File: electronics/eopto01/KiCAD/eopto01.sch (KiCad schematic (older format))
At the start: 7 parts, among them K1 CONN_3, Q1 BC849

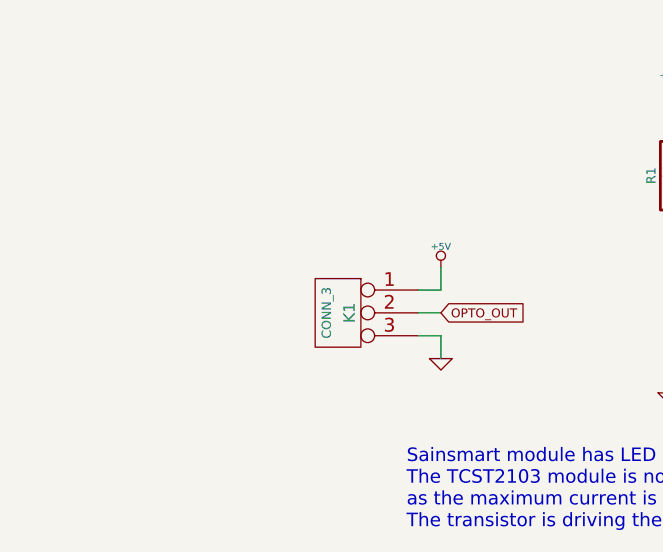
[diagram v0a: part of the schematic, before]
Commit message: Added JST connector for Opto-endstop
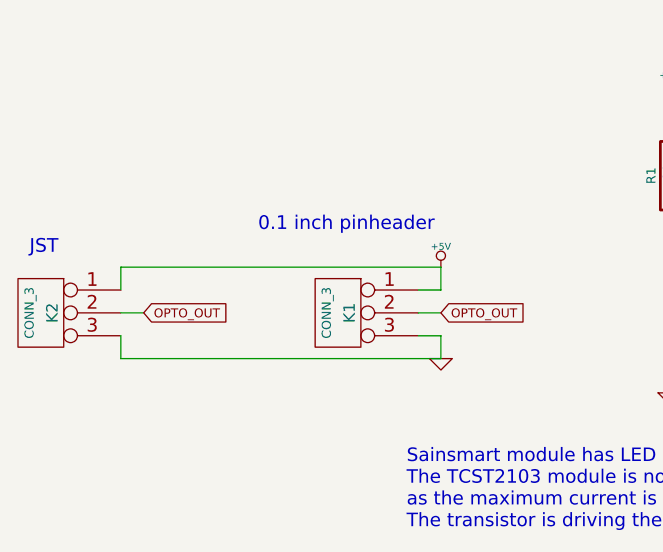
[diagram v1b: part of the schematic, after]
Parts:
- added K2: CONN_3, symbol CONN_3
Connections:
- net +5V: now also K2.1 (P1)
- net GND: now also K2.3 (P3)
- net OPTO_OUT: now also K2.2 (PM)
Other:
- note added: "0.1 inch pinheader"
- note added: "JST"
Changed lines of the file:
@@
 LIBS:valves
 LIBS:lerchetech
+LIBS:eopto01-cache
 EELAYER 27 0
 EELAYER END
@@
 Sheet 1 1
 Title "FirePick - Opto endstop board"
-Date "9 jul 2014"
+Date "12 jul 2014"
 Rev "A"
 Comp "FirePick"
@@
 Text Notes 4050 4750 0    59   ~ 0
 Sainsmart module has LED connected directly to opto-transistor output. \nThe TCST2103 module is not able to supply the current for the red LED, \nas the maximum current is 4mA @ 20mA forward current on the infrared LED. \nThe transistor is driving the LED, so when the light is interrupted, the LED lights up.
+$Comp
+L CONN_3 K2
+U 1 1 53C19586
+P 2450 3800
+F 0 "K2" V 2400 3800 50  0000 C CNN
+F 1 "CONN_3" V 2500 3800 40  0000 C CNN
+F 2 "" H 2450 3800 60  0000 C CNN
+F 3 "" H 2450 3800 60  0000 C CNN
+	1    2450 3800
+	-1   0    0    -1
+$EndComp
+Wire Wire Line
+	4200 3600 2800 3600
+Wire Wire Line
+	4200 4000 2800 4000
+Wire Wire Line
+	2800 3600 2800 3700
+Wire Wire Line
+	2800 4000 2800 3900
+Wire Wire Line
+	2800 3800 2900 3800
+Text GLabel 2900 3800 2    39   Input ~ 0
+OPTO_OUT
+Text Notes 2400 3550 0    60   ~ 0
+JST
+Text Notes 3400 3450 0    60   ~ 0
+0.1 inch pinheader
 $EndSCHEMATC

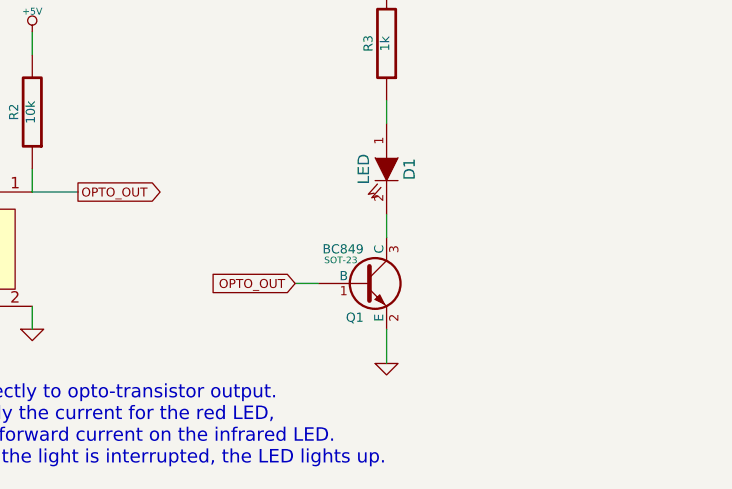
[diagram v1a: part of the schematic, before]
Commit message: Changed to MOSFET for LED
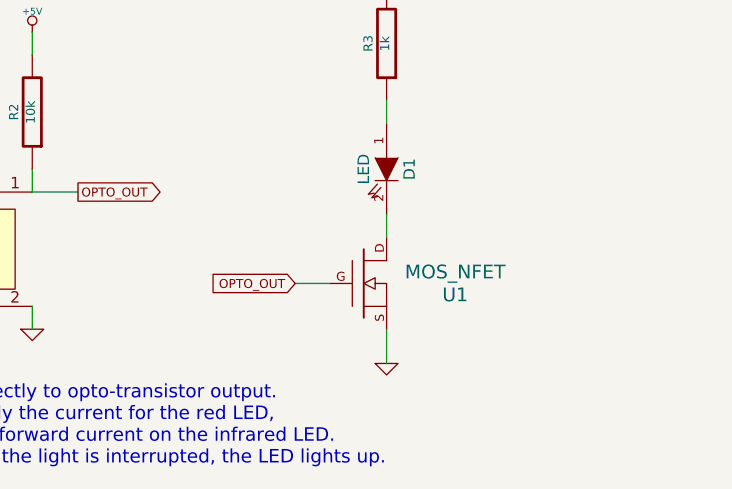
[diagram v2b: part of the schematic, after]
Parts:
- removed Q1: BC849, SOT-23, symbol BC849
- added U1: MOS_NFET, ~, symbol MOS_NFET
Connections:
- net GND: now also U1.2 (S)
- net OPTO_OUT: now also U1.1 (G)
- net at D1.2 (K): now also U1.3 (D)
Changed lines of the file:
@@
 Sheet 1 1
 Title "FirePick - Opto endstop board"
-Date "12 jul 2014"
+Date "26 sep 2014"
 Rev "A"
 Comp "FirePick"
@@
 Wire Wire Line
 	5900 4050 5900 4150
-$Comp
-L BC849 Q1
-U 1 1 53BD4106
-P 7350 3950
-F 0 "Q1" H 7350 3801 40  0000 R CNN
-F 1 "BC849" H 7350 4100 40  0000 R CNN
-F 2 "SOT-23" H 7250 4052 29  0000 C CNN
-F 3 "~" H 7350 3950 60  0000 C CNN
-	1    7350 3950
-	1    0    0    -1
-$EndComp
 Wire Wire Line
 	5900 3550 6100 3550
@@
 OPTO_OUT
 Wire Wire Line
-	7150 3950 7050 3950
+	7050 3950 7200 3950
 Text GLabel 7050 3950 0    39   Input ~ 0
 OPTO_OUT
@@
 Text Notes 3400 3450 0    60   ~ 0
 0.1 inch pinheader
+$Comp
+L MOS_NFET U1
+U 1 1 5425E7F0
+P 7350 3950
+F 0 "U1" H 7750 3900 60  0000 C CNN
+F 1 "MOS_NFET" H 7750 4000 60  0000 C CNN
+F 2 "~" H 7450 3950 60  0000 C CNN
+F 3 "~" H 7450 3950 60  0000 C CNN
+	1    7350 3950
+	1    0    0    -1
+$EndComp
 $EndSCHEMATC
